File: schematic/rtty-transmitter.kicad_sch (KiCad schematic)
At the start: 71 parts, among them J1 USB Type B Connector, J2 USBasp header, J3 Conn_Coaxial, J4 Conn_01x02_Pin, J5 Conn_01x02_Pin, J6 Conn_01x02_Pin, Q1 PN2222A, Q2 PN2222A, U1 MCP2221AxP, U2 ATmega328P-P, U3 MCP4901, U4 MCP6022, U5 2x5 Pin Header Connector Fema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, U6 25LC1024, Y1 16 MHz

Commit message: Schematic: Test points and annotation updated
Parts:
- TP1: renamed from TP3; value TestPoint -> Virtual Ground; footprint TestPoint:TestPoint_Plated_Hole_D2.0mm -> TestPoint:TestPoint_THTPad_D1.0mm_Drill0.5mm
- TP2: renamed from TP4; value TestPoint -> GND; footprint TestPoint:TestPoint_Plated_Hole_D2.0mm -> TestPoint:TestPoint_THTPad_D1.0mm_Drill0.5mm
- TP3: renamed from TP1; value TestPoint -> Carrier Wave; footprint TestPoint:TestPoint_Plated_Hole_D2.0mm -> TestPoint:TestPoint_THTPad_D1.0mm_Drill0.5mm
- TP4: renamed from TP2; value TestPoint -> Buffered Audio; footprint TestPoint:TestPoint_Plated_Hole_D2.0mm -> TestPoint:TestPoint_THTPad_D1.0mm_Drill0.5mm
- renumbered C5 to C1, C13 to C10, C8 to C11, C14 to C12, C10 to C13, C9 to C14, C19 to C16, C16 to C18, C18 to C19, C1 to C2, C6 to C3, C2 to C5, C12 to C6, C11 to C7, C7 to C8, C3 to C9, D2 to D1, D1 to D2, U5 to J3, J3 to J7, R6 to R12, R8 to R13, R18 to R15, R19 to R16, R24 to R17, R22 to R18, R16 to R19, R21 to R20, R23 to R21, R17 to R22, R15 to R23, R20 to R24, R4 to R3, R3 to R4, R7 to R6, R12 to R7, R13 to R8, U6 to U4, U4 to U5
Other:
- note added: "Microcontroller circuit (USB to Serial conversion, AT command parsing, RTTY signal generation)"
- note removed: "Microcontroller circuit"
- moved on the sheet: C17, C19, R15, R16, TP1, TP2, U5C

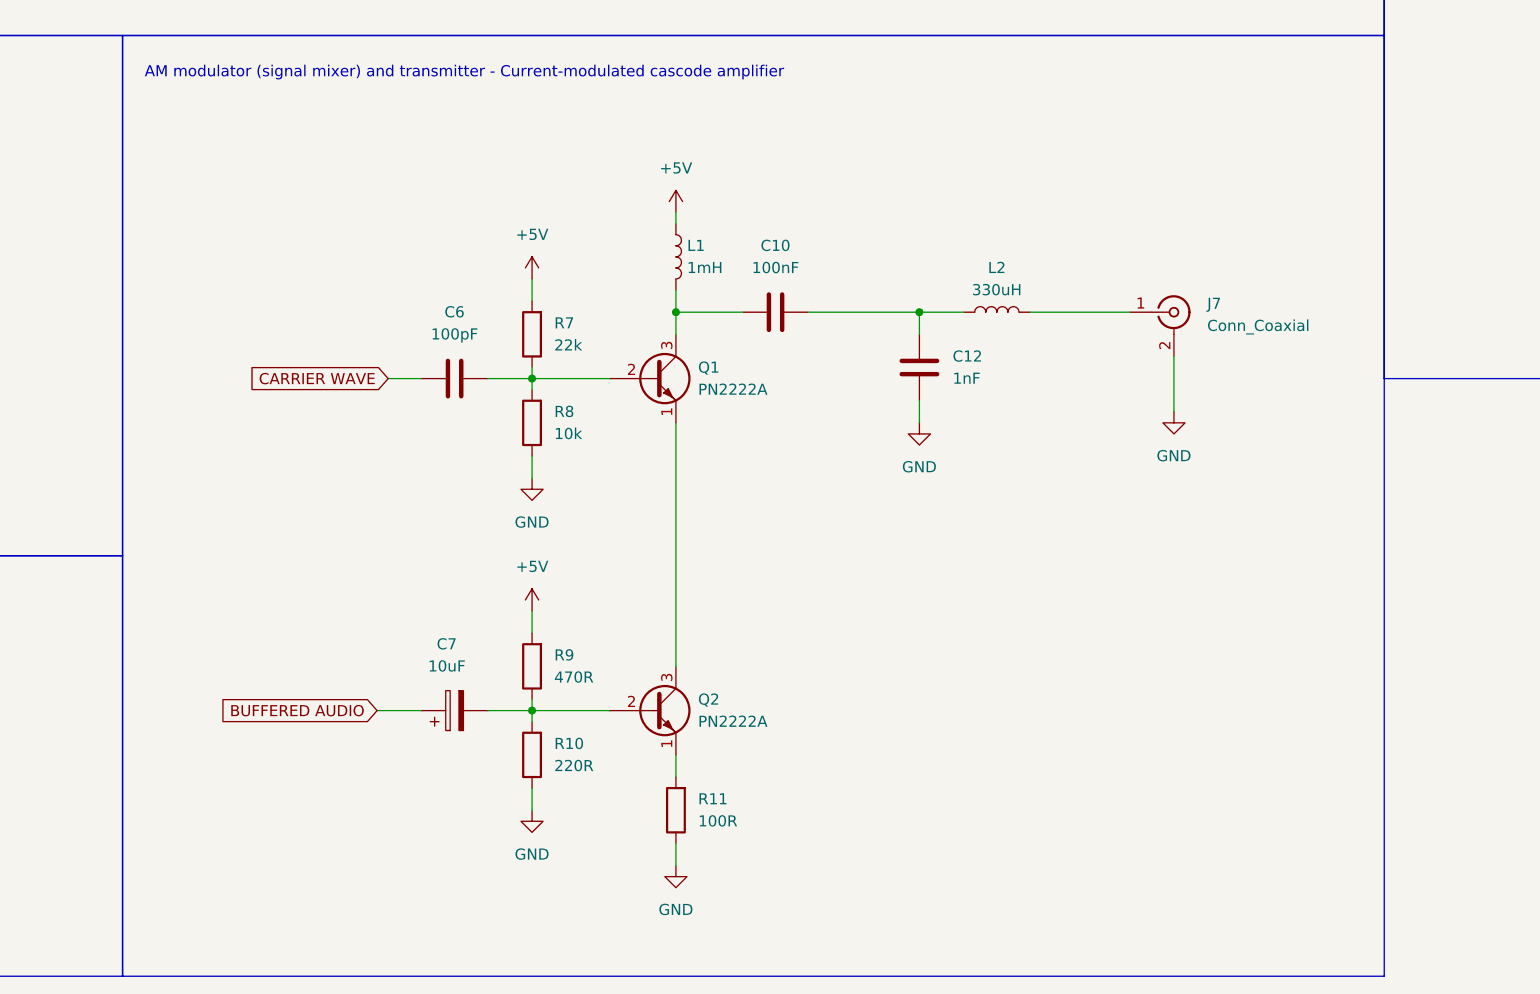
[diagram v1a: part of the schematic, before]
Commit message: PCB: SMA connector updated
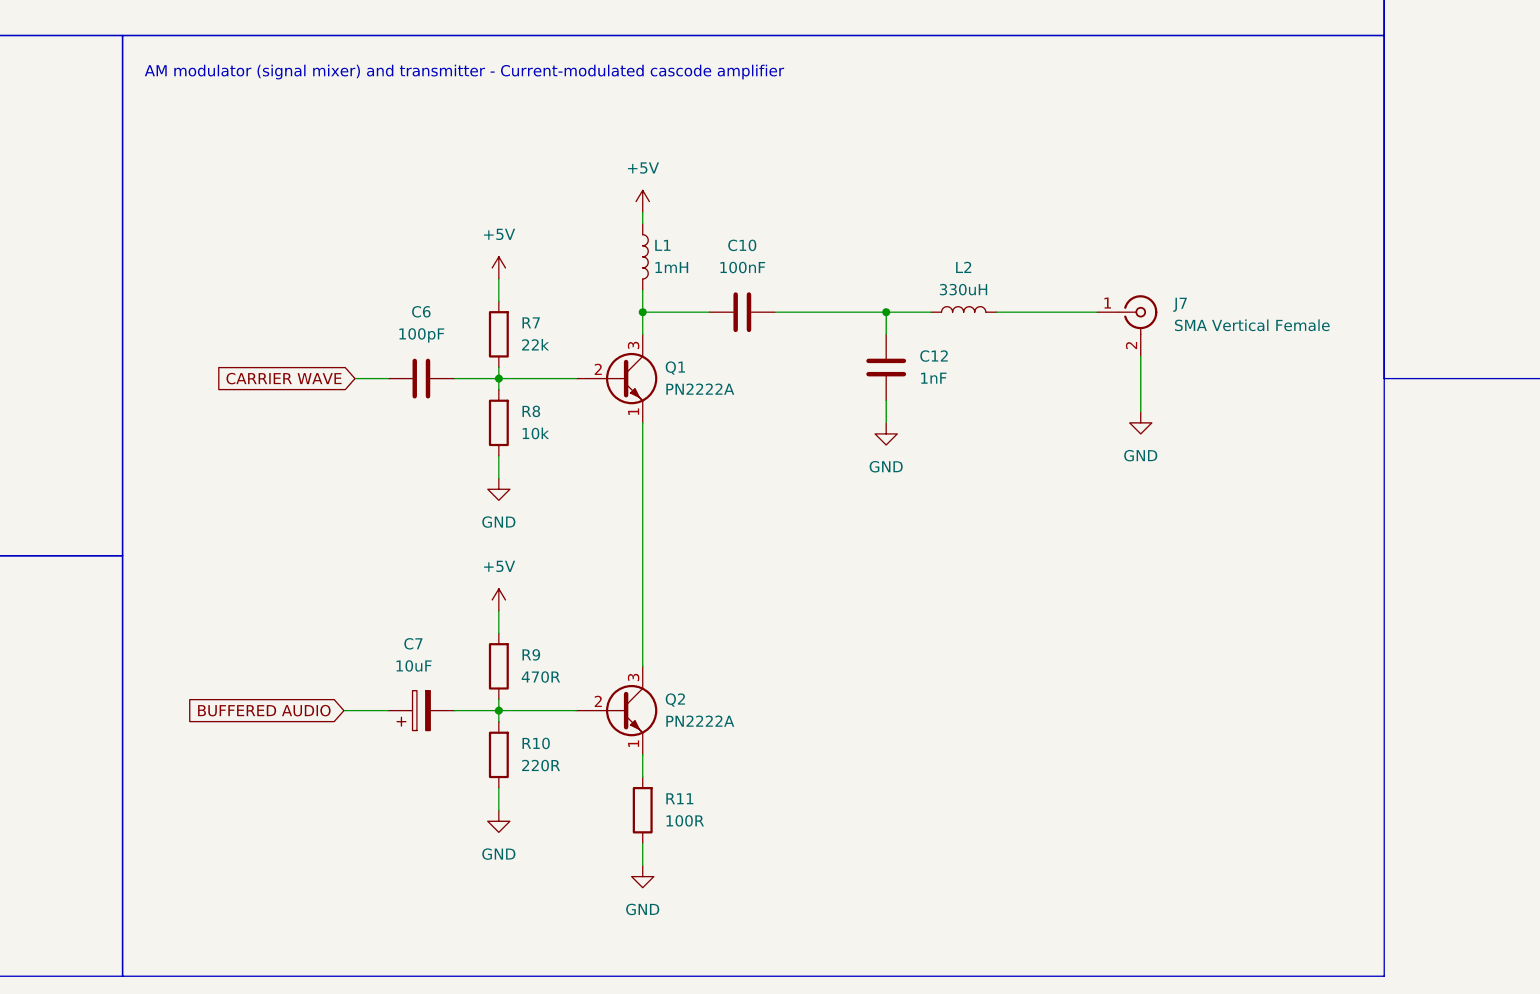
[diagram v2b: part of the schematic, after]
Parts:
- removed J7: Conn_Coaxial, Connector_Coaxial:SMA_Amphenol_901-144_Vertical, symbol Connector:Conn_Coaxial
- added J7: SMA Vertical Female, StockLib:SMA Vertical Female, symbol StockLib:SMA Vertical Female
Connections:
- net GND: now also J7.2 (Ext)
- net at L2.2: now also J7.1 (In)
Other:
- moved on the sheet: C10, C12, C6, C7, L1, L2, Q1, Q2, R10, R11, R7, R8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

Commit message: PCB updated: electrolytic capacitor footprints updated
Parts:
- C13, C16, C17, C3, C7: footprint Capacitor_THT:CP_Radial_D6.3mm_P2.50mm -> Capacitor_THT:CP_Radial_D5.0mm_P2.00mm
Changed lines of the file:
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@@
       (effects (font (size 1.27 1.27)) (justify left))
     )
-    (property "Footprint" "Capacitor_THT:CP_Radial_D6.3mm_P2.50mm" (at 122.8852 46.99 0)
+    (property "Footprint" "Capacitor_THT:CP_Radial_D5.0mm_P2.00mm" (at 122.8852 46.99 0)
       (effects (font (size 1.27 1.27)) hide)
     )
@@
       (effects (font (size 1.27 1.27)))
     )
-    (property "Footprint" "Capacitor_THT:CP_Radial_D6.3mm_P2.50mm" (at 327.66 172.4152 0)
+    (property "Footprint" "Capacitor_THT:CP_Radial_D5.0mm_P2.00mm" (at 327.66 172.4152 0)
       (effects (font (size 1.27 1.27)) hide)
     )
@@
       (effects (font (size 1.27 1.27)))
     )
-    (property "Footprint" "Capacitor_THT:CP_Radial_D6.3mm_P2.50mm" (at 246.38 53.6448 0)
+    (property "Footprint" "Capacitor_THT:CP_Radial_D5.0mm_P2.00mm" (at 246.38 53.6448 0)
       (effects (font (size 1.27 1.27)) hide)
     )
@@
       (effects (font (size 1.27 1.27)))
     )
-    (property "Footprint" "Capacitor_THT:CP_Radial_D6.3mm_P2.50mm" (at 176.53 246.6848 0)
+    (property "Footprint" "Capacitor_THT:CP_Radial_D5.0mm_P2.00mm" (at 176.53 246.6848 0)
       (effects (font (size 1.27 1.27)) hide)
     )
@@
       (effects (font (size 1.27 1.27)) (justify left))
     )
-    (property "Footprint" "Capacitor_THT:CP_Radial_D6.3mm_P2.50mm" (at 346.4052 55.88 0)
-      (effects (font (size 1.27 1.27)) hide)
-    )
+    (property "Footprint" "Capacitor_THT:CP_Radial_D5.0mm_P2.00mm" (at 346.4052 55.88 0)
+      (effects (font (size 1.27 1.27)) hide)
+    )

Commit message: PCB updated: resistor footprints updated
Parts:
- R9: footprint StockLib:R_10k_Axial_DIN0207 -> StockLib:R_470_Axial_DIN0207
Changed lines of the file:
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@@
       (effects (font (size 1.27 1.27)) (justify right))
     )
-    (property "Footprint" "StockLib:R_10k_Axial_DIN0207" (at 183.388 242.57 90)
+    (property "Footprint" "StockLib:R_470_Axial_DIN0207" (at 183.388 242.57 90)
       (effects (font (size 1.27 1.27)) hide)
     )
